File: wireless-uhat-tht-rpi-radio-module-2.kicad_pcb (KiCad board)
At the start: 2 copper layers, 65 x 30 mm, 16 parts, among them J1 GPIO, J2 DEBUG

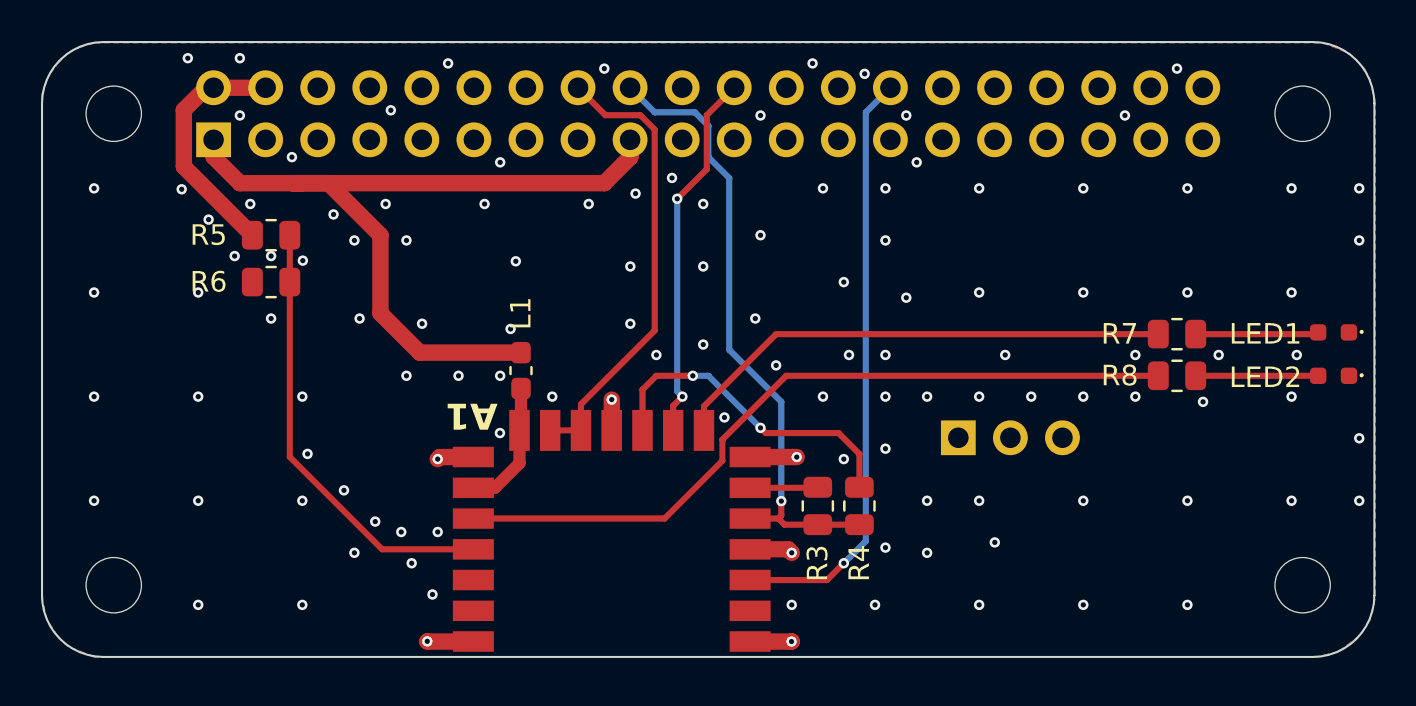
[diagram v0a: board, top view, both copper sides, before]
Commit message: tl;dr: finishing touches to send board in for prototyping
=======================================================================
added:
  gerbers/
      wireless-uhat-tht-rpi-radio-module-2.7z - forgot to remove before
        commit

-----------------------------------------------------------------------
modified:
  gerbers/  - regenerated to reflect updates
      wireless-uhat-tht-rpi-radio-module-2-B_Cu.gbl
      wireless-uhat-tht-rpi-radio-module-2-B_Mask.gbs
      wireless-uhat-tht-rpi-radio-module-2-B_Paste.gbp
      wireless-uhat-tht-rpi-radio-module-2-B_Silkscreen.gbo
      wireless-uhat-tht-rpi-radio-module-2-Edge_Cuts.gm1
      wireless-uhat-tht-rpi-radio-module-2-F_Cu.gtl
      wireless-uhat-tht-rpi-radio-module-2-F_Mask.gts
      wireless-uhat-tht-rpi-radio-module-2-F_Paste.gtp
      wireless-uhat-tht-rpi-radio-module-2-F_Silkscreen.gto
      wireless-uhat-tht-rpi-radio-module-2-NPTH-drl_map.gbr
      wireless-uhat-tht-rpi-radio-module-2-NPTH.drl
      wireless-uhat-tht-rpi-radio-module-2-PTH-drl_map.gbr
      wireless-uhat-tht-rpi-radio-module-2-PTH.drl
      wireless-uhat-tht-rpi-radio-module-2-job.gbrjob

  ./    - updated fonts, removed debug connector (will remove from
    mainboard if needed)
      wireless-uhat-tht-rpi-radio-module-2.kicad_pcb
      wireless-uhat-tht-rpi-radio-module-2.kicad_prl
      wireless-uhat-tht-rpi-radio-module-2.kicad_pro
      wireless-uhat-tht-rpi-radio-module-2.kicad_sch

-----------------------------------------------------------------------
renamed:
  misc/wireless-uhat-tht-rpi-radio-module-2.csv
      -> misc/wireless-uhat-tht-rpi-radio-module-2_BOM.csv
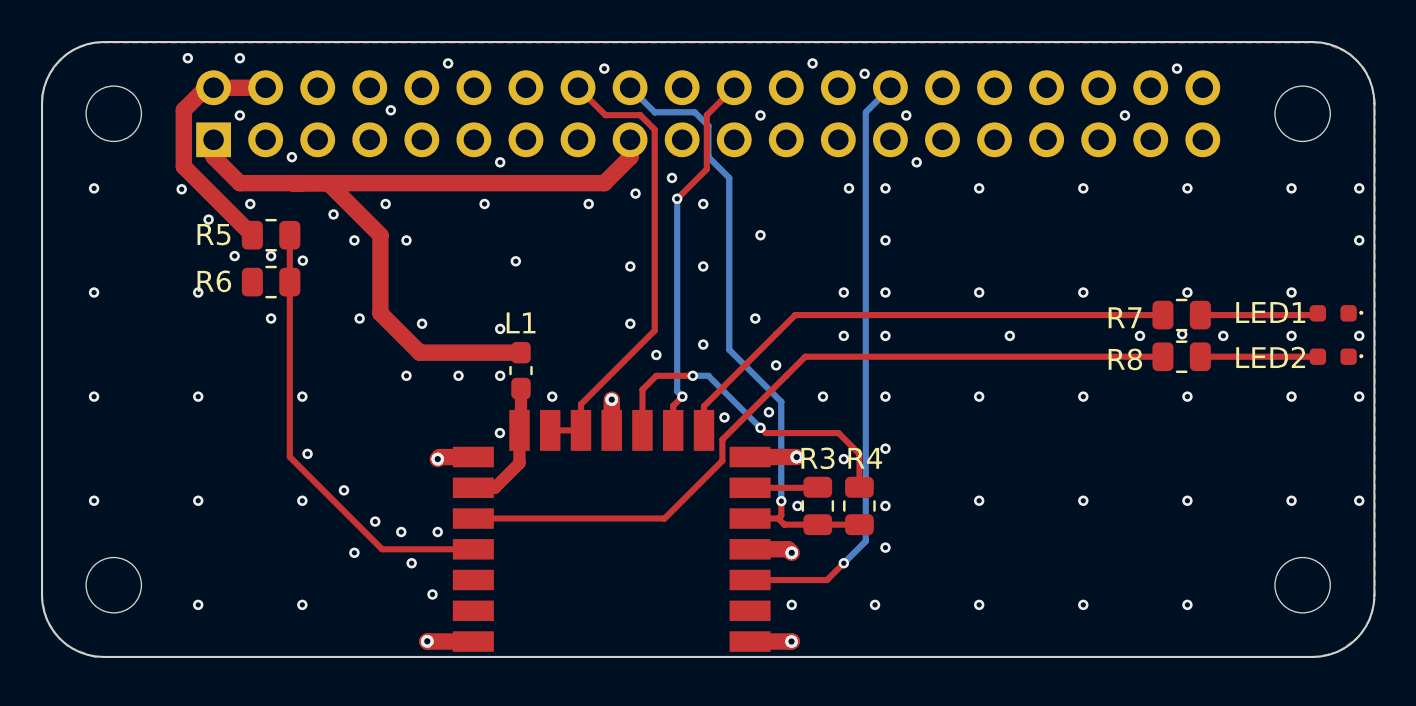
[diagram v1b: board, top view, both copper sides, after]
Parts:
- removed J2: DEBUG, Connector_PinSocket_2.54mm:PinSocket_1x03_P2.54mm_Vertical
- moved R8 0.96 mm to (155.6, 85.4)
- moved R7 0.96 mm to (155.6, 83.3)
- moved LED2 0.93 mm to (163.0, 85.4)
- moved LED1 0.93 mm to (163.0, 83.2)
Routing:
- net /WL_GPIO2: track 36.9 -> 37.5 mm
- net /WL_GPIO0: track 24.8 -> 25.4 mm
- net GND: vias 121 -> 120
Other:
- board text added: "DEBUG OPENING?"

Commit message: tl;dr: added fonts, moved RM2 module, switched to CC by-SA 4.0 license
=======================================================================
added:
  ./
      LICENSE - switched to CC by-SA license
  .kinotes/
      wireless-uhat-tht-rpi-radio-module-2_worklog_20260220.md - am i
        supposed to be writing in this?  whoops

-----------------------------------------------------------------------
removed:
  ./
      fp-info-cache - finally remembered to untrack
      wireless-uhat-tht-rpi-radio-module-2.kicad_prl - same

-----------------------------------------------------------------------
modified:
  ./
      wireless-uhat-tht-rpi-radio-module-2.kicad_pcb - changed layout
        of board to move RM2 module safely within the board outline.  i
        haven't even gotten the 0.0.0 prototype yet so i hope i have to
        fix something else even more major later
      wireless-uhat-tht-rpi-radio-module-2.kicad_pro - rev -> 0.1.1 or
        something
      wireless-uhat-tht-rpi-radio-module-2.kicad_sch - removed eeprom
        section and debug connector

  .kinotes/
      settings.json - i should probably untrack this, who cares

  gerbers/
      wireless-uhat-tht-rpi-radio-module-2* - updated with fonts and new
        pcb layout

-----------------------------------------------------------------------
moved:
  ./wireless-uhat-tht-rpi-radio-module-2.kicad_* - rev 0.0.0
      -> r0-0-0/wireless-uhat-tht-rpi-radio-module-2.kicad_*

  .kinotes/KiNotes_wireless-uhat-rpi-radio-module-2.md
      -> r0-0-0/.kinotes/KiNotes_wireless-uhat-rpi-radio-module-2.md

  gerbers/wireless-uhat-tht-rpi-radio-module-2* - rev 0.0.0
      -> r0-0-0/gerbers/wireless-uhat-tht-rpi-radio-module-2*

  "but Cat, that's stupid? just use git version control FFS!"
      -> That is unfortunate.

-----------------------------------------------------------------------
renamed:
  .kinotes/KiNotes_wireless-uhat-rpi-radio-module-2.md
      -> .kinotes/KiNotes_wireless-uhat-tht-rpi-radio-module-2.m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
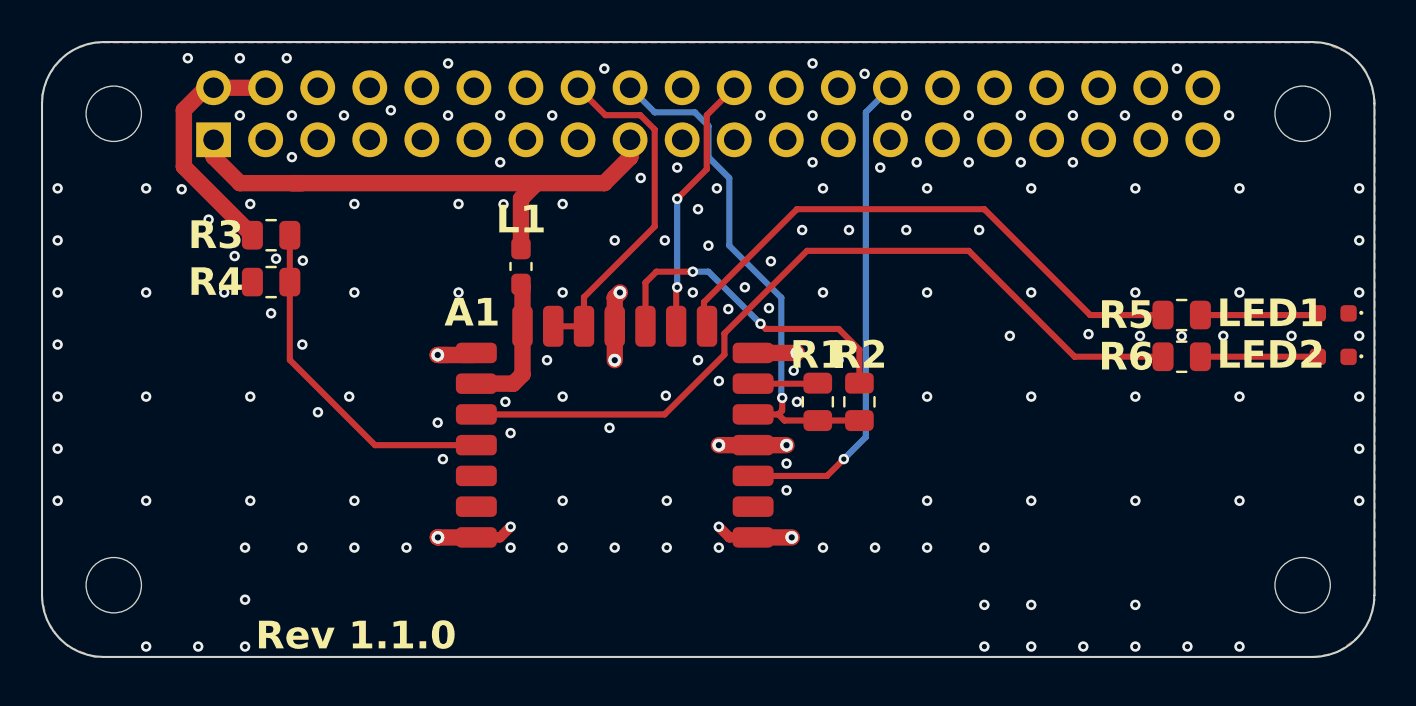
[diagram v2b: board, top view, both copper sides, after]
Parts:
- moved R3 44.6 mm to (111.2, 79.4), turned to 0 degrees
- moved R4 44.6 mm to (111.2, 81.7)
- moved R2 29.3 mm to (139.9, 87.6), turned to 90 degrees
- moved R1 27.9 mm to (137.8, 87.6), turned to 90 degrees
- moved R5 20.0 mm to (155.6, 83.3), turned to 180 degrees
- moved R6 17.3 mm to (155.6, 85.4), turned to 180 degrees
- moved A1 5.08 mm to (127.9, 91.6)
- moved L1 5.08 mm to (123.4, 81.0)
- moved LED2 2.12 mm to (163.0, 85.4)
- moved LED1 2.12 mm to (163.0, 83.2)
- renumbered LED2 to LED1, LED1 to LED2, R5 to R1, R6 to R2, R7 to R3, R8 to R4, R3 to R5, R4 to R6
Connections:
- LED1 pad 2: Net-(LED2-A) -> Net-(LED1-A)
- LED2 pad 2: Net-(LED1-A) -> Net-(LED2-A)
- R1 pad 1: +5V -> /GPIO24
- R1 pad 2: /WL_GPIO1 -> Net-(A1-DO)
- R2 pad 1: /WL_GPIO1 -> /GPIO24
- R2 pad 2: GND -> Net-(A1-nIRQ)
- R3 pad 1: Net-(LED1-A) -> +5V
- R3 pad 2: /WL_GPIO0 -> /WL_GPIO1
- R4 pad 1: Net-(LED2-A) -> /WL_GPIO1
- R4 pad 2: /WL_GPIO2 -> GND
- R5 pad 1: /GPIO24 -> Net-(LED1-A)
- R5 pad 2: Net-(A1-DO) -> /WL_GPIO0
- R6 pad 1: /GPIO24 -> Net-(LED2-A)
- R6 pad 2: Net-(A1-nIRQ) -> /WL_GPIO2
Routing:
- net +3V3: track 40.4 -> 27.1 mm
- net GND: track 11.9 -> 18.8 mm, vias 120 -> 164
- net /GPIO25: track 18.2 -> 12.8 mm
- net /GPIO1: track 29.1 -> 23.8 mm
- net /GPIO23: track 22.3 -> 17.1 mm
- net /GPIO24: track 30.7 -> 25.7 mm
- net /WL_GPIO1: track 21.6 -> 16.9 mm
- net /WL_GPIO0: track 25.4 -> 27.6 mm
- net /WL_GPIO2: track 37.5 -> 39.5 mm
- net Net-(A1-VDDIO): track 6.32 -> 6.86 mm
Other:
- board text added: "Rev ${REVISION}"

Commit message: tl;dr: debug connector zone was marked on the WRONG SIDE of the BOARD FFS moved RM2 further
=======================================================================
removed:
  .kinotes/
      wireless-uhat-rpi-radio-module-2_worklog_20260213.md - old

-----------------------------------------------------------------------
modified:
  ./
      README.md - typo
      wireless-uhat-tht-rpi-radio-module-2.kicad_pcb - had debug opening
        marked on wrong side of the board :(

  .kinotes/
      KiNotes_wireless-uhat-tht-rpi-radio-module-2.md - typo

  gerbers/
      wireless-uhat-tht-rpi-radio-module-2-* - updated -> rev 1.2.0
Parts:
- moved A1 5.08 mm to (133.0, 91.6)
- moved L1 5.08 mm to (128.4, 81.0)
- moved R2 5.08 mm to (145.0, 87.6)
- moved R1 5.08 mm to (142.9, 87.6)
- moved R3 0.25 mm to (111.2, 79.2)
- moved R4 0.25 mm to (111.2, 81.5)
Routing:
- net /WL_GPIO0: track 27.6 -> 21.0 mm
- net /WL_GPIO1: track 16.9 -> 23.3 mm
- net /WL_GPIO2: track 39.5 -> 33.4 mm
- net /GPIO24: track 25.7 -> 28.8 mm
- net GND: track 18.8 -> 17.4 mm, vias 164 -> 171
- net /GPIO1: track 23.8 -> 22.6 mm
- net /GPIO25: track 12.8 -> 13.8 mm
- net /GPIO23: track 17.1 -> 16.4 mm
- net +5V: track 11.9 -> 12.5 mm
